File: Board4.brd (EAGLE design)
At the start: 75.5 x 94.9 mm, 20 parts, among them IC1 MEGA8-P, P1 Serial, P2 I2C, P3 Buzzer, P4 ISP_WANNENBUCHSE, P7 Test, Q1 BSS101, Q4 BSS101, U1 100nF, U2 100uF, U4 100nF

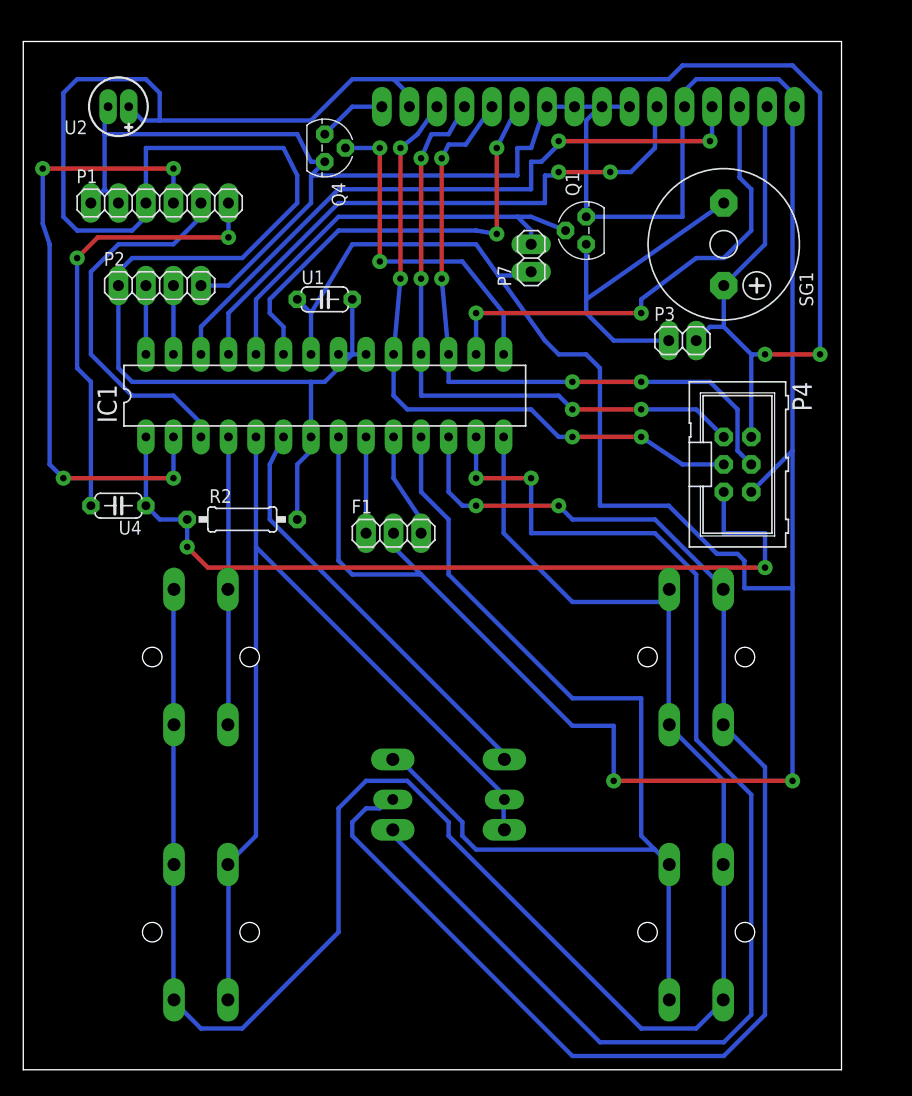
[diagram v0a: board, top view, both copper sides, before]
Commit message: bug in pcb fixed
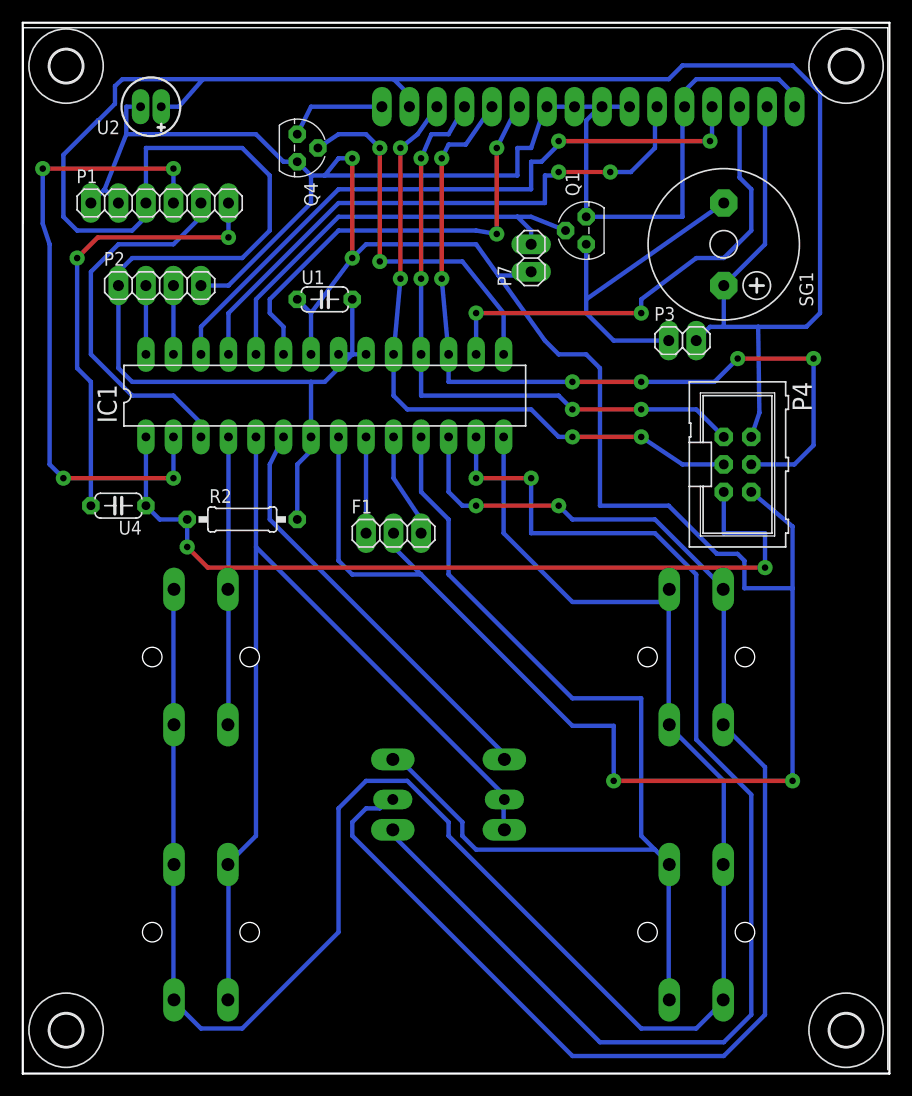
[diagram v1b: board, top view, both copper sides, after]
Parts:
- added U$1, U$2, U$3, U$4: (no value), holes:3,0
- moved U2 3.00 mm to (39.8, 95.2)
- moved Q4 2.54 mm to (53.3, 91.4)
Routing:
- net GND: track 346.6 -> 316.0 mm, vias 2 -> 4
- net LCD_DB5: track 61.2 -> 77.0 mm, vias 4 -> 6
- net 5V: track 266.7 -> 255.5 mm, vias 2 -> 0
- net LCD_BACKLIGHT: track 31.2 -> 34.6 mm
- net N$2: track 6.32 -> 9.38 mm
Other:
- board size 75.5 x 94.9 mm -> 80 x 97 mm
